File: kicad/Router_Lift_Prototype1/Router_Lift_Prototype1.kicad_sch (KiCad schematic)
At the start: 31 parts

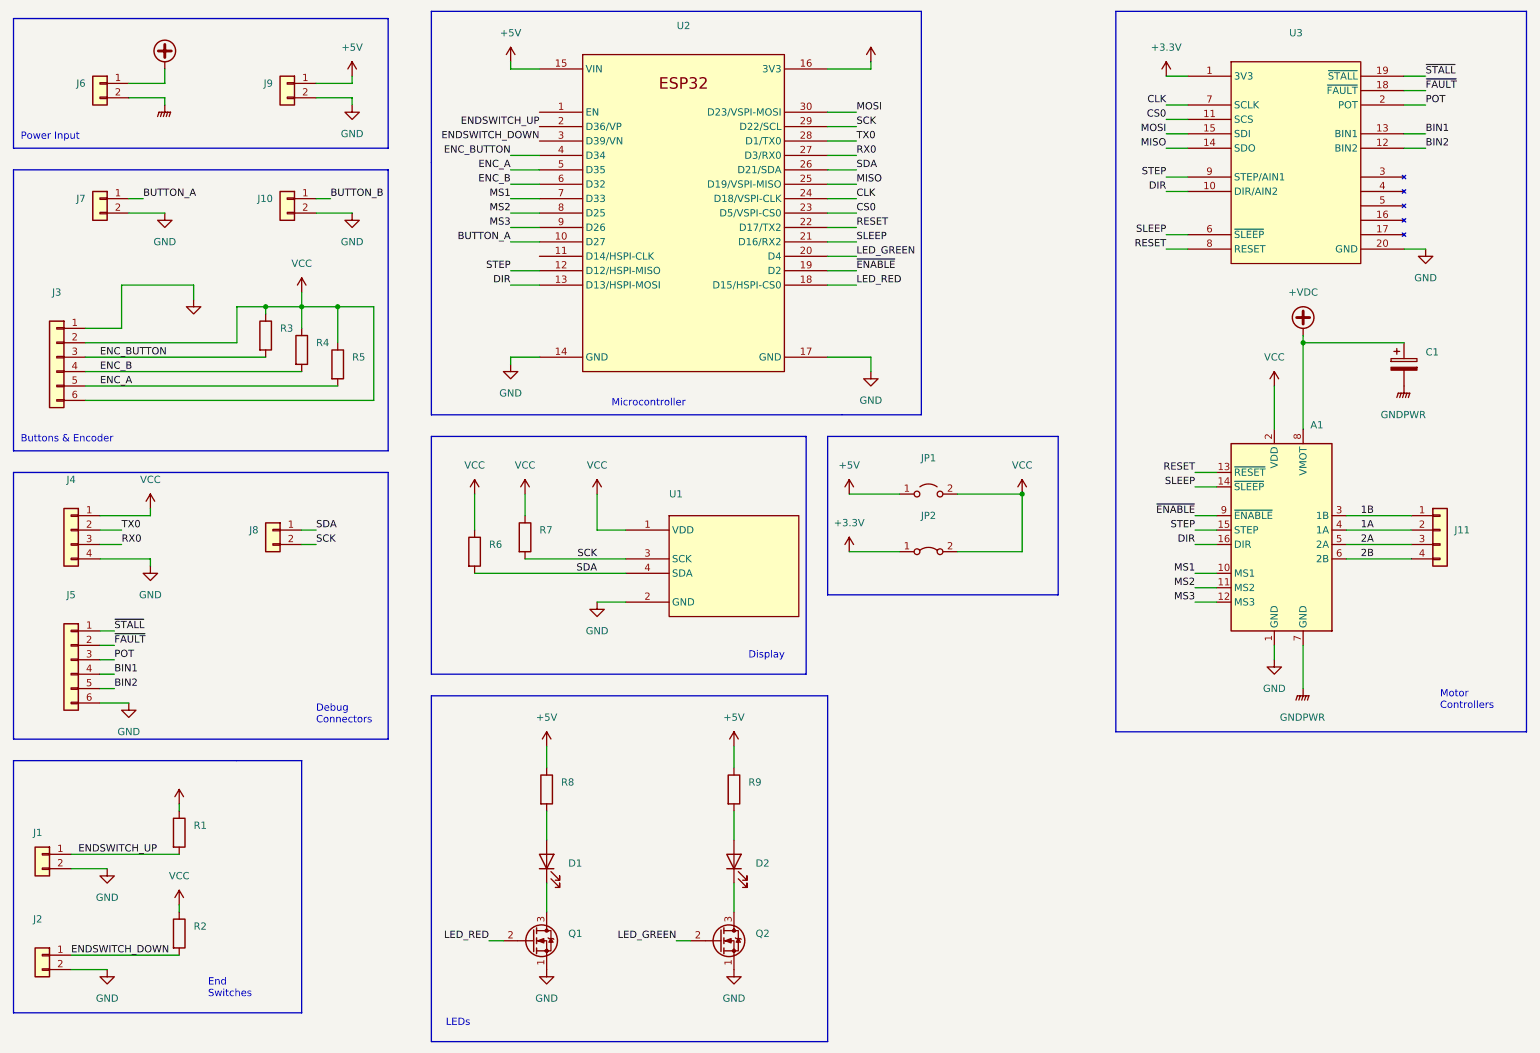
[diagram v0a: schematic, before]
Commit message: Linked further footprints and first placing
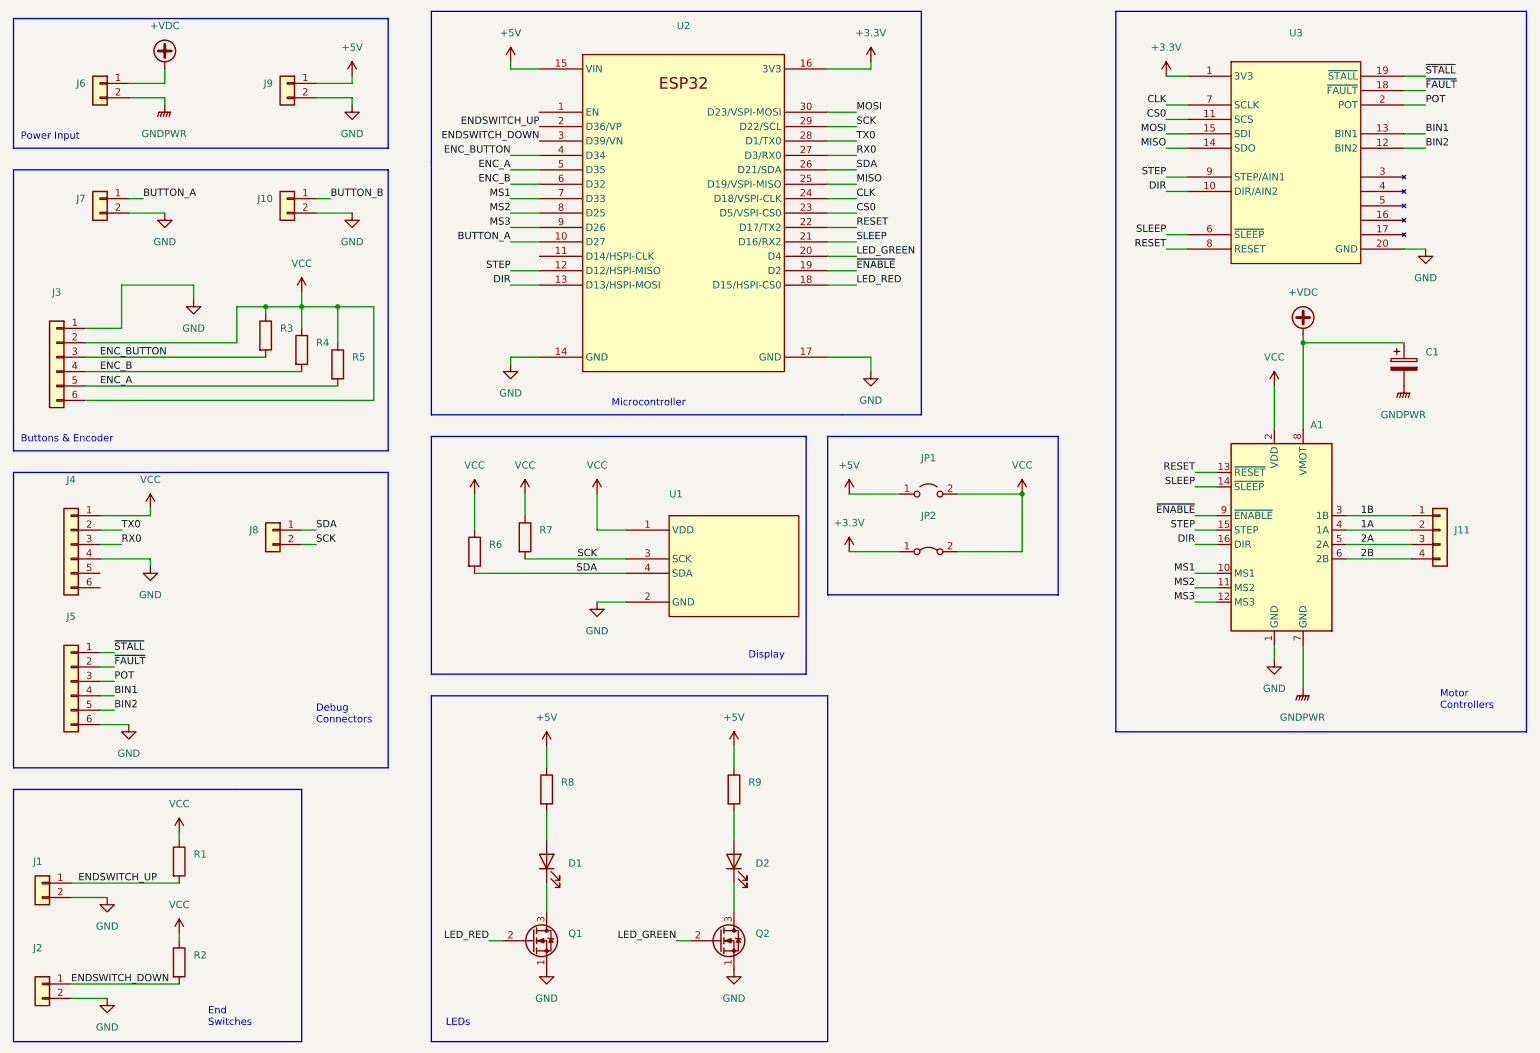
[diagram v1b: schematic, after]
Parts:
- removed J4: (no value), symbol Connector_Generic:Conn_01x04
- added J4: (no value), symbol Connector_Generic:Conn_01x06
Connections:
- net GND: now also J4.4 (Pin_4)
- net RX0: now also J4.3 (Pin_3)
- net TX0: now also J4.2 (Pin_2)
- net VCC: now also J4.1 (Pin_1)
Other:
- moved on the sheet: J1, J2, J5, R1, R2

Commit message: Completing Layout - Several Pin changes to be updated in Software
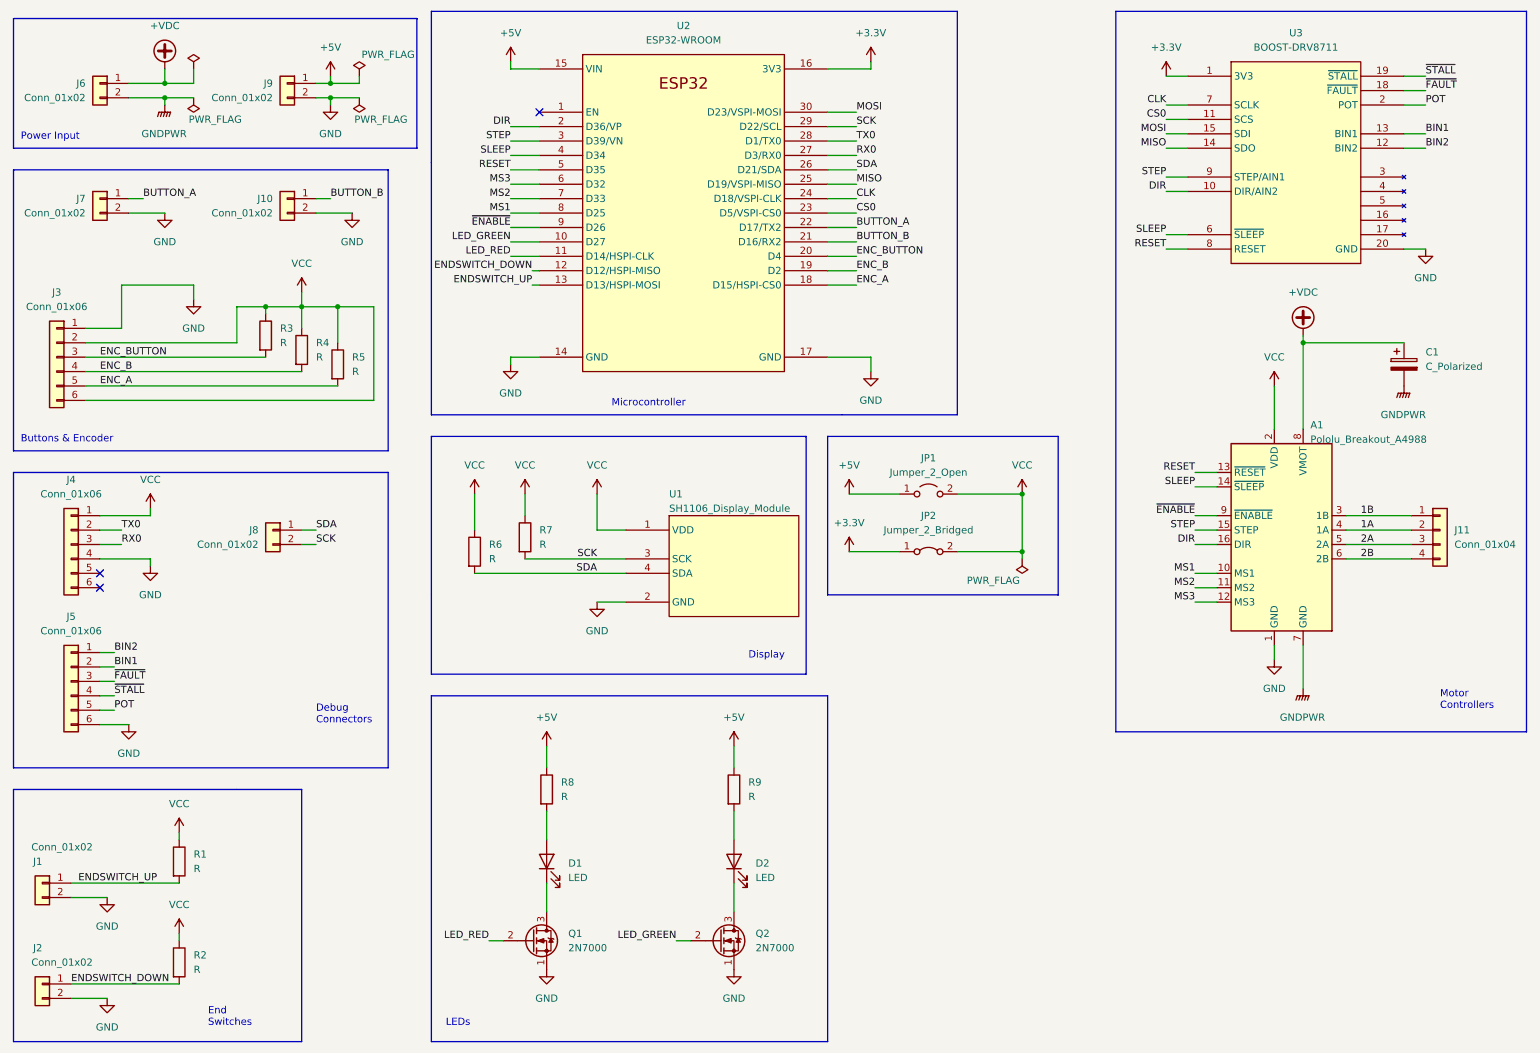
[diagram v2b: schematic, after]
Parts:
- A1: value (none) -> Pololu_Breakout_A4988; footprint (none) -> Module:Pololu_Breakout-16_15.2x20.3mm
- C1: value (none) -> C_Polarized; footprint (none) -> Capacitor_THT:CP_Radial_D6.3mm_P2.50mm
- D1, D2: value (none) -> LED; footprint (none) -> LED_THT:LED_D3.0mm
- J1, J10, J2, J6, J7, J8, J9: value (none) -> Conn_01x02; footprint (none) -> TerminalBlock_TE-Connectivity:TerminalBlock_TE_282834-2_1x02_P2.54mm_Horizontal
- J11: value (none) -> Conn_01x04; footprint (none) -> TerminalBlock_TE-Connectivity:TerminalBlock_TE_282834-4_1x04_P2.54mm_Horizontal
- J3, J4, J5: value (none) -> Conn_01x06; footprint (none) -> TerminalBlock_TE-Connectivity:TerminalBlock_TE_282834-6_1x06_P2.54mm_Horizontal
- JP1: value (none) -> Jumper_2_Open; footprint (none) -> Connector_PinHeader_2.54mm:PinHeader_1x02_P2.54mm_Vertical
- JP2: value (none) -> Jumper_2_Bridged; footprint (none) -> Connector_PinHeader_2.54mm:PinHeader_1x02_P2.54mm_Vertical
- Q1, Q2: value (none) -> 2N7000; footprint (none) -> Package_TO_SOT_THT:TO-92_Inline
- R1, R2, R3, R4, R5, R6, R7, R8, R9: value (none) -> R; footprint (none) -> Resistor_THT:R_Axial_DIN0207_L6.3mm_D2.5mm_P10.16mm_Horizontal
- U1: value (none) -> SH1106_Display_Module; footprint (none) -> Display:SH1106_Makershop
- U2: value (none) -> ESP32-WROOM; footprint (none) -> ESP32-DevKits:ESP32-WROOM
- U3: value (none) -> BOOST-DRV8711; footprint (none) -> Module:TI_BOOST_DRV8711
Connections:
- net BIN1: now also J5.2 (Pin_2); no longer J5.4 (Pin_4)
- net BIN2: now also J5.1 (Pin_1); no longer J5.5 (Pin_5)
- net BUTTON_A: now also U2.22 (D17/TX2); no longer U2.10 (D27)
- net BUTTON_B: now also U2.21 (D16/RX2)
- net DIR: now also U2.2 (D36/VP); no longer U2.13 (D13/HSPI-MOSI)
- net ENC_A: now also U2.18 (D15/HSPI-CS0); no longer U2.5 (D35)
- net ENC_B: now also U2.19 (D2); no longer U2.6 (D32)
- net ENC_BUTTON: now also U2.20 (D4); no longer U2.4 (D34)
- net ENDSWITCH_DOWN: now also U2.12 (D12/HSPI-MISO); no longer U2.3 (D39/VN)
- net ENDSWITCH_UP: now also U2.13 (D13/HSPI-MOSI); no longer U2.2 (D36/VP)
- net LED_GREEN: now also U2.10 (D27); no longer U2.20 (D4)
- net LED_RED: now also U2.11 (D14/HSPI-CLK); no longer U2.18 (D15/HSPI-CS0)
- net MS1: now also U2.8 (D25); no longer U2.7 (D33)
- net MS2: now also U2.7 (D33); no longer U2.8 (D25)
- net MS3: now also U2.6 (D32); no longer U2.9 (D26)
- net POT: now also J5.5 (Pin_5); no longer J5.3 (Pin_3)
- net RESET: now also U2.5 (D35); no longer U2.22 (D17/TX2)
- net SLEEP: now also U2.4 (D34); no longer U2.21 (D16/RX2)
- net STEP: now also U2.3 (D39/VN); no longer U2.12 (D12/HSPI-MISO)
- net ~{ENABLE}: now also U2.9 (D26); no longer U2.19 (D2)
- net ~{FAULT}: now also J5.3 (Pin_3); no longer J5.2 (Pin_2)
- net ~{STALL}: now also J5.4 (Pin_4); no longer J5.1 (Pin_1)
- no-connect marks 0 -> 3
